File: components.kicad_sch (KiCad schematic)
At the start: 11 parts, among them J3 Conn_01x03, Q1 2N2222, U5 74AHCT1G125

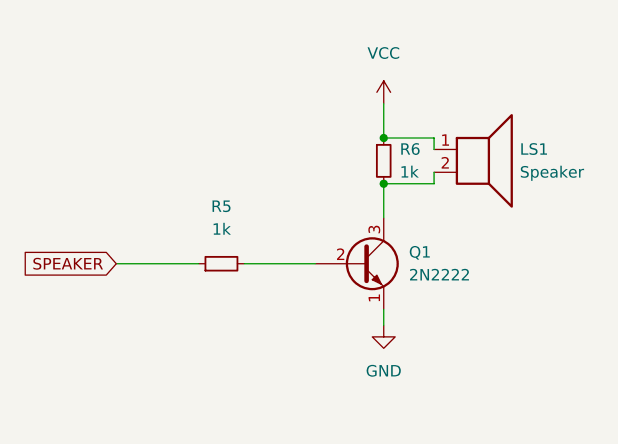
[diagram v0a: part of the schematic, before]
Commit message: switch and matrix components placed
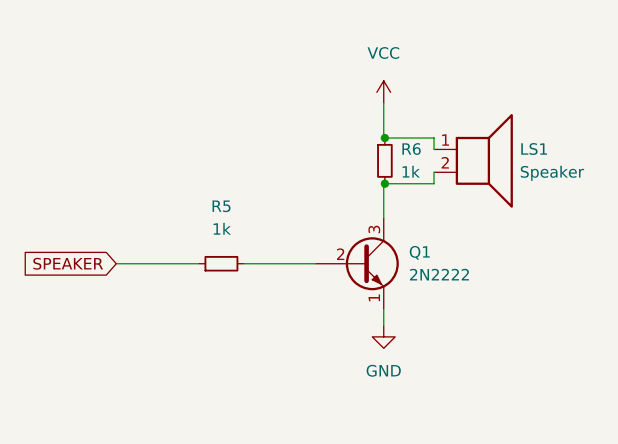
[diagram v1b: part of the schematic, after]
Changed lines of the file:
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@@
 (kicad_sch (version 20230121) (generator eeschema)
   (paper "A4")
-  (junction (at 159.893 41.91) (diameter 0) (color 0 0 0 0)
-  )
   (junction (at 90.17 71.755) (diameter 0) (color 0 0 0 0)
   )
-  (junction (at 159.893 36.83) (diameter 0) (color 0 0 0 0)
+  (junction (at 160.02 41.91) (diameter 0) (color 0 0 0 0)
   )
   (junction (at 90.17 79.375) (diameter 0) (color 0 0 0 0)
   )
+  (junction (at 160.02 36.83) (diameter 0) (color 0 0 0 0)
+  )
   (wire (pts (xy 86.995 50.165) (xy 92.075 50.165))
     (stroke (width 0) (type default))
@@
     (stroke (width 0) (type default))
   )
-  (wire (pts (xy 159.893 41.91) (xy 165.481 41.91))
+  (wire (pts (xy 159.893 41.91) (xy 160.02 41.91))
     (stroke (width 0) (type default))
   )
@@
     (stroke (width 0) (type default))
   )
+  (wire (pts (xy 160.02 41.91) (xy 165.481 41.91))
+    (stroke (width 0) (type default))
+  )
   (wire (pts (xy 165.481 38.1) (xy 165.481 36.83))
     (stroke (width 0) (type default))
@@
     (stroke (width 0) (type default))
   )
-  (wire (pts (xy 165.481 36.83) (xy 159.893 36.83))
+  (wire (pts (xy 165.481 36.83) (xy 160.02 36.83))
     (stroke (width 0) (type default))
   )
   (wire (pts (xy 86.995 52.705) (xy 92.075 52.705))
+    (stroke (width 0) (type default))
+  )
+  (wire (pts (xy 160.02 36.83) (xy 159.893 36.83))
     (stroke (width 0) (type default))
   )
@@
     )
   )
-  (symbol (lib_id "Device:R_Small") (at 159.893 39.37 0) (unit 1)
-    (in_bom yes) (on_board yes) (dnp no) (fields_autoplaced)
-    (property "Reference" "R6" (at 161.671 38.0999 0)
-      (effects (font (size 1.27 1.27)) (justify left))
-    )
-    (property "Value" "1k" (at 161.671 40.6399 0)
-      (effects (font (size 1.27 1.27)) (justify left))
-    )
-    (property "Footprint" "Resistor_SMD:R_0402_1005Metric" (at 159.893 39.37 0)
-      (effects (font (size 1.27 1.27)) hide)
-    )
-    (property "Datasheet" "~" (at 159.893 39.37 0)
-      (effects (font (size 1.27 1.27)) hide)
-    )
+  (symbol (lib_id "Device:R_Small") (at 160.02 39.37 0) (unit 1)
+    (in_bom yes) (on_board yes) (dnp no) (fields_autoplaced)
+    (property "Reference" "R6" (at 161.798 38.0999 0)
+      (effects (font (size 1.27 1.27)) (justify left))
+    )
+    (property "Value" "1k" (at 161.798 40.6399 0)
+      (effects (font (size 1.27 1.27)) (justify left))
+    )
+    (property "Footprint" "Resistor_SMD:R_0402_1005Metric" (at 160.02 39.37 0)
+      (effects (font (size 1.27 1.27)) hide)
+    )
+    (property "Datasheet" "~" (at 160.02 39.37 0)
+      (effects (font (size 1.27 1.27)) hide)
+    )

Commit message: added STEM project WIP
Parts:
- R6, R8, R9: footprint Resistor_SMD:R_0402_1005Metric -> Resistor_SMD:R_0603_1608Metric
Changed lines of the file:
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@@
     (pin "1")
     (instances
-      (project "Didaktik rp2040"
+      (project "Didaktik STEM"
         (path "/6e18f33c-52fd-4500-abcd-bacc1810501e"
           (reference "#PWR0120") (unit 1)
@@
     (pin "2")
     (instances
-      (project "Didaktik rp2040"
+      (project "Didaktik STEM"
         (path "/6e18f33c-52fd-4500-abcd-bacc1810501e"
           (reference "LS1") (unit 1)
@@
     (pin "2")
     (instances
-      (project "Didaktik rp2040"
+      (project "Didaktik STEM"
         (path "/6e18f33c-52fd-4500-abcd-bacc1810501e"
           (reference "R5") (unit 1)
@@
     (pin "1")
     (instances
-      (project "Didaktik rp2040"
+      (project "Didaktik STEM"
         (path "/6e18f33c-52fd-4500-abcd-bacc1810501e"
           (reference "#PWR0126") (unit 1)
@@
     (pin "1")
     (instances
-      (project "Didaktik rp2040"
+      (project "Didaktik STEM"
         (path "/6e18f33c-52fd-4500-abcd-bacc1810501e/45857a2d-aa8d-4210-86ca-38a01efddb7c"
           (reference "#PWR038") (unit 1)
@@
     (pin "5")
     (instances
-      (project "Didaktik rp2040"
+      (project "Didaktik STEM"
         (path "/6e18f33c-52fd-4500-abcd-bacc1810501e/45857a2d-aa8d-4210-86ca-38a01efddb7c"
           (reference "U5") (unit 1)
@@
     (pin "2")
     (instances
-      (project "Didaktik rp2040"
+      (project "Didaktik STEM"
         (path "/6e18f33c-52fd-4500-abcd-bacc1810501e"
           (reference "D43") (unit 1)
@@
       (effects (font (size 1.27 1.27)) (justify left))
     )
-    (property "Footprint" "Resistor_SMD:R_0402_1005Metric" (at 48.895 43.815 0)
+    (property "Footprint" "Resistor_SMD:R_0603_1608Metric" (at 48.895 43.815 0)
       (effects (font (size 1.27 1.27)) hide)
     )
@@
     (pin "2")
     (instances
-      (project "Didaktik rp2040"
+      (project "Didaktik STEM"
         (path "/6e18f33c-52fd-4500-abcd-bacc1810501e"
           (reference "R9") (unit 1)
@@
     (pin "2")
     (instances
-      (project "Didaktik rp2040"
+      (project "Didaktik STEM"
         (path "/6e18f33c-52fd-4500-abcd-bacc1810501e/45857a2d-aa8d-4210-86ca-38a01efddb7c"
           (reference "C1") (unit 1)
@@
     (pin "1")
     (instances
-      (project "Didaktik rp2040"
+      (project "Didaktik STEM"
         (path "/6e18f33c-52fd-4500-abcd-bacc1810501e"
           (reference "#PWR0122") (unit 1)
@@
       (effects (font (size 1.27 1.27)) (justify left))
     )
-    (property "Footprint" "Resistor_SMD:R_0402_1005Metric" (at 160.02 39.37 0)
+    (property "Footprint" "Resistor_SMD:R_0603_1608Metric" (at 160.02 39.37 0)
       (effects (font (size 1.27 1.27)) hide)
     )
@@
     (pin "2")
     (instances
-      (project "Didaktik rp2040"
+      (project "Didaktik STEM"
         (path "/6e18f33c-52fd-4500-abcd-bacc1810501e"
           (reference "R6") (unit 1)
@@
     (pin "3")
     (instances
-      (project "Didaktik rp2040"
+      (project "Didaktik STEM"
         (path "/6e18f33c-52fd-4500-abcd-bacc1810501e"
           (reference "Q1") (unit 1)
@@
     (pin "1")
     (instances
-      (project "Didaktik rp2040"
+      (project "Didaktik STEM"
         (path "/6e18f33c-52fd-4500-abcd-bacc1810501e/45857a2d-aa8d-4210-86ca-38a01efddb7c"
           (reference "#PWR037") (unit 1)
@@
     (pin "1")
     (instances
-      (project "Didaktik rp2040"
+      (project "Didaktik STEM"
         (path "/6e18f33c-52fd-4500-abcd-bacc1810501e/45857a2d-aa8d-4210-86ca-38a01efddb7c"
           (reference "#PWR039") (unit 1)
@@
     (pin "1")
     (instances
-      (project "Didaktik rp2040"
+      (project "Didaktik STEM"
         (path "/6e18f33c-52fd-4500-abcd-bacc1810501e"
           (reference "#PWR0123") (unit 1)
@@
     (pin "3")
     (instances
-      (project "Didaktik rp2040"
+      (project "Didaktik STEM"
         (path "/6e18f33c-52fd-4500-abcd-bacc1810501e"
           (reference "J3") (unit 1)
@@
     (pin "1")
     (instances
-      (project "Didaktik rp2040"
+      (project "Didaktik STEM"
         (path "/6e18f33c-52fd-4500-abcd-bacc1810501e"
           (reference "#PWR0125") (unit 1)
@@
     (pin "1")
     (instances
-      (project "Didaktik rp2040"
+      (project "Didaktik STEM"
         (path "/6e18f33c-52fd-4500-abcd-bacc1810501e/45857a2d-aa8d-4210-86ca-38a01efddb7c"
           (reference "#PWR040") (unit 1)
@@
     (pin "2")
     (instances
-      (project "Didaktik rp2040"
+      (project "Didaktik STEM"
         (path "/6e18f33c-52fd-4500-abcd-bacc1810501e"
           (reference "D42") (unit 1)
@@
       (effects (font (size 1.27 1.27)) (justify left))
     )
-    (property "Footprint" "Resistor_SMD:R_0402_1005Metric" (at 36.195 43.815 0)
+    (property "Footprint" "Resistor_SMD:R_0603_1608Metric" (at 36.195 43.815 0)
       (effects (font (size 1.27 1.27)) hide)
     )
@@
     (pin "2")
     (instances
-      (project "Didaktik rp2040"
+      (project "Didaktik STEM"
         (path "/6e18f33c-52fd-4500-abcd-bacc1810501e"
           (reference "R8") (unit 1)
